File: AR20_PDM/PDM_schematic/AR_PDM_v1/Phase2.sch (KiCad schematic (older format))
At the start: 10 parts, among them Q6 BTS50025-1TAD, U6 INA233

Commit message: Working on pcb layout
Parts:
- removed D?: D_Schottky_x2, symbol AR20_PDM_v1-rescue:D_Schottky_x2
- added D51, D52: D_Schottky_BAT60A, AR_PDM_v1:D_Shotky_BAT60_HandSoldering, symbol AR20_PDM_v1-rescue:D_Schottky_BAT60A
- gave numbers to parts that had none: 4
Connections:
- net GND: now also D51.2 (A), D52.2 (A)
- net at R113.1, U6.10 (IN+): now also D52.1 (K)
- net at R111.1, U6.9 (In-): now also D51.1 (K)
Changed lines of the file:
@@
 AR Path="/5E0E594B/5EE88A56" Ref="R?"  Part="1"
 AR Path="/5E0E607C/5EE88A56" Ref="R?"  Part="1"
-AR Path="/5E0FB5C8/5EE88A56" Ref="R?"  Part="1"
+AR Path="/5E0FB5C8/5EE88A56" Ref="R112"  Part="1"
 AR Path="/5E0FBBBD/5EE88A56" Ref="R?"  Part="1"
 AR Path="/5E0FC3A2/5EE88A56" Ref="R?"  Part="1"
@@
 AR Path="/5E0FDCCC/5EE88A56" Ref="R?"  Part="1"
 AR Path="/5E10174B/5EE88A56" Ref="R?"  Part="1"
-F 0 "R?" V 6643 1600 50  0000 C CNN
+F 0 "R112" V 6643 1600 50  0000 C CNN
 F 1 "2m_1%_4W" V 6734 1600 50  0000 C CNN
 F 2 "Resistor_SMD:R_2512_6332Metric" V 6780 1600 50  0001 C CNN
@@
 Text HLabel 7300 1600 2    50   Input ~ 10
 V+12V
-$Comp
-L AR20_PDM_v1-rescue:D_Schottky_x2 D?
-U 1 1 5EE88A5D
-P 6950 4825
-AR Path="/5DA89415/5EE88A5D" Ref="D?"  Part="1"
-AR Path="/5E0FB5C8/5EE88A5D" Ref="D?"  Part="1"
-F 0 "D?" H 6950 5041 50  0000 C CNN
-F 1 "D_Schottky_x2" H 6950 4950 50  0000 C CNN
-F 2 "" H 6950 4825 50  0001 C CNN
-F 3 "~" H 6950 4825 50  0001 C CNN
-	1    6950 4825
-	1    0    0    -1
-$EndComp
 $Comp
 L AR20_PDM_v1-rescue:R-Device R?
@@
 AR Path="/5E0E594B/5EE88A63" Ref="R?"  Part="1"
 AR Path="/5E0E607C/5EE88A63" Ref="R?"  Part="1"
-AR Path="/5E0FB5C8/5EE88A63" Ref="R?"  Part="1"
+AR Path="/5E0FB5C8/5EE88A63" Ref="R111"  Part="1"
 AR Path="/5E0FBBBD/5EE88A63" Ref="R?"  Part="1"
 AR Path="/5E0FC3A2/5EE88A63" Ref="R?"  Part="1"
@@
 AR Path="/5E0FDCCC/5EE88A63" Ref="R?"  Part="1"
 AR Path="/5E10174B/5EE88A63" Ref="R?"  Part="1"
-F 0 "R?" V 6443 3850 50  0000 C CNN
+F 0 "R111" V 6443 3850 50  0000 C CNN
 F 1 "1K_1%" V 6534 3850 50  0000 C CNN
 F 2 "Resistor_SMD:R_0603_1608Metric" V 6580 3850 50  0001 C CNN
@@
 AR Path="/5E0E594B/5EE88A69" Ref="R?"  Part="1"
 AR Path="/5E0E607C/5EE88A69" Ref="R?"  Part="1"
-AR Path="/5E0FB5C8/5EE88A69" Ref="R?"  Part="1"
+AR Path="/5E0FB5C8/5EE88A69" Ref="R113"  Part="1"
 AR Path="/5E0FBBBD/5EE88A69" Ref="R?"  Part="1"
 AR Path="/5E0FC3A2/5EE88A69" Ref="R?"  Part="1"
@@
 AR Path="/5E0FDCCC/5EE88A69" Ref="R?"  Part="1"
 AR Path="/5E10174B/5EE88A69" Ref="R?"  Part="1"
-F 0 "R?" V 6843 3850 50  0000 C CNN
+F 0 "R113" V 6843 3850 50  0000 C CNN
 F 1 "1K_1%" V 6934 3850 50  0000 C CNN
 F 2 "Resistor_SMD:R_0603_1608Metric" V 6980 3850 50  0001 C CNN
@@
 Text Notes 7075 2000 0    50   ~ 10
 Place shunt and INA233 close, \nroute togethere, differentialy pair. \nKeep short, and away from Noise.
-$Comp
-L AR20_PDM_v1-rescue:GND-power #PWR?
-U 1 1 5EE88A77
-P 6950 5025
-AR Path="/5DA89415/5EE88A77" Ref="#PWR?"  Part="1"
-AR Path="/5DEB10A1/5EE88A77" Ref="#PWR?"  Part="1"
-AR Path="/5DEB20EA/5EE88A77" Ref="#PWR?"  Part="1"
-AR Path="/5E0E4725/5EE88A77" Ref="#PWR?"  Part="1"
-AR Path="/5E0E4A93/5EE88A77" Ref="#PWR?"  Part="1"
-AR Path="/5E0E4EB5/5EE88A77" Ref="#PWR?"  Part="1"
-AR Path="/5E0E5304/5EE88A77" Ref="#PWR?"  Part="1"
-AR Path="/5E0E594B/5EE88A77" Ref="#PWR?"  Part="1"
-AR Path="/5E0E607C/5EE88A77" Ref="#PWR?"  Part="1"
-AR Path="/5E0FB5C8/5EE88A77" Ref="#PWR?"  Part="1"
-AR Path="/5E0FBBBD/5EE88A77" Ref="#PWR?"  Part="1"
-AR Path="/5E0FC3A2/5EE88A77" Ref="#PWR?"  Part="1"
-AR Path="/5E0FCFDC/5EE88A77" Ref="#PWR?"  Part="1"
-AR Path="/5E0FDCCC/5EE88A77" Ref="#PWR?"  Part="1"
-AR Path="/5E10174B/5EE88A77" Ref="#PWR?"  Part="1"
-F 0 "#PWR?" H 6950 4775 50  0001 C CNN
-F 1 "GND" H 6955 4852 50  0000 C CNN
-F 2 "" H 6950 5025 50  0001 C CNN
-F 3 "" H 6950 5025 50  0001 C CNN
-	1    6950 5025
-	1    0    0    -1
-$EndComp
 Wire Wire Line
 	4775 1600 6650 1600
@@
 Wire Wire Line
 	6650 4400 8750 4400
-Connection ~ 6650 4400
-Wire Wire Line
-	6650 4400 6650 4825
-Wire Wire Line
-	8750 4300 7250 4300
-Wire Wire Line
-	7250 4825 7250 4300
-Connection ~ 7250 4300
-Wire Wire Line
-	7250 4300 7050 4300
 $Comp
 L AR20_PDM_v1-rescue:R-Device R?
@@
 AR Path="/5E0E594B/5EEC0C80" Ref="R?"  Part="1"
 AR Path="/5E0E607C/5EEC0C80" Ref="R?"  Part="1"
-AR Path="/5E0FB5C8/5EEC0C80" Ref="R?"  Part="1"
+AR Path="/5E0FB5C8/5EEC0C80" Ref="R114"  Part="1"
 AR Path="/5E0FBBBD/5EEC0C80" Ref="R?"  Part="1"
 AR Path="/5E0FC3A2/5EEC0C80" Ref="R?"  Part="1"
@@
 AR Path="/5E0FDCCC/5EEC0C80" Ref="R?"  Part="1"
 AR Path="/5E10174B/5EEC0C80" Ref="R?"  Part="1"
-F 0 "R?" V 8093 4100 50  0000 C CNN
+F 0 "R114" V 8093 4100 50  0000 C CNN
 F 1 "10K" V 8184 4100 50  0000 C CNN
 F 2 "Resistor_SMD:R_0603_1608Metric" V 8230 4100 50  0001 C CNN
@@
 Text HLabel 8150 4100 0    50   Output ~ 10
 P2_OUT
+Wire Wire Line
+	7050 4300 7100 4300
+$Comp
+L AR20_PDM_v1-rescue:D_Schottky_BAT60A D?
+U 1 1 5EFA1E07
+P 6700 4775
+AR Path="/5DA89415/5EFA1E07" Ref="D?"  Part="1"
+AR Path="/5E0FB5C8/5EFA1E07" Ref="D51"  Part="1"
+F 0 "D51" V 6530 4885 50  0000 L CNN
+F 1 "D_Schottky_BAT60A" V 6621 4885 50  0000 L CNN
+F 2 "AR_PDM_v1:D_Shotky_BAT60_HandSoldering" H 6800 4725 50  0001 C CNN
+F 3 "~" H 6800 4725 50  0001 C CNN
+	1    6700 4775
+	0    1    1    0
+$EndComp
+$Comp
+L AR20_PDM_v1-rescue:GND-power #PWR?
+U 1 1 5EFA1E0D
+P 6875 4950
+AR Path="/5DA89415/5EFA1E0D" Ref="#PWR?"  Part="1"
+AR Path="/5DEB10A1/5EFA1E0D" Ref="#PWR?"  Part="1"
+AR Path="/5DEB20EA/5EFA1E0D" Ref="#PWR?"  Part="1"
+AR Path="/5E0E4725/5EFA1E0D" Ref="#PWR?"  Part="1"
+AR Path="/5E0E4A93/5EFA1E0D" Ref="#PWR?"  Part="1"
+AR Path="/5E0E4EB5/5EFA1E0D" Ref="#PWR?"  Part="1"
+AR Path="/5E0E5304/5EFA1E0D" Ref="#PWR?"  Part="1"
+AR Path="/5E0E594B/5EFA1E0D" Ref="#PWR?"  Part="1"
+AR Path="/5E0E607C/5EFA1E0D" Ref="#PWR?"  Part="1"
+AR Path="/5E0FB5C8/5EFA1E0D" Ref="#PWR013"  Part="1"
+AR Path="/5E0FBBBD/5EFA1E0D" Ref="#PWR?"  Part="1"
+AR Path="/5E0FC3A2/5EFA1E0D" Ref="#PWR?"  Part="1"
+AR Path="/5E0FCFDC/5EFA1E0D" Ref="#PWR?"  Part="1"
+AR Path="/5E0FDCCC/5EFA1E0D" Ref="#PWR?"  Part="1"
+AR Path="/5E10174B/5EFA1E0D" Ref="#PWR?"  Part="1"
+F 0 "#PWR013" H 6875 4700 50  0001 C CNN
+F 1 "GND" H 6880 4777 50  0000 C CNN
+F 2 "" H 6875 4950 50  0001 C CNN
+F 3 "" H 6875 4950 50  0001 C CNN
+	1    6875 4950
+	1    0    0    -1
+$EndComp
+$Comp
+L AR20_PDM_v1-rescue:D_Schottky_BAT60A D?
+U 1 1 5EFA1E13
+P 7150 4775
+AR Path="/5DA89415/5EFA1E13" Ref="D?"  Part="1"
+AR Path="/5E0FB5C8/5EFA1E13" Ref="D52"  Part="1"
+F 0 "D52" V 6980 4885 50  0000 L CNN
+F 1 "D_Schottky_BAT60A" V 7071 4885 50  0000 L CNN
+F 2 "AR_PDM_v1:D_Shotky_BAT60_HandSoldering" H 7250 4725 50  0001 C CNN
+F 3 "~" H 7250 4725 50  0001 C CNN
+	1    7150 4775
+	0    1    1    0
+$EndComp
+Wire Wire Line
+	6650 4475 6650 4400
+Wire Wire Line
+	7100 4475 7100 4300
+Wire Wire Line
+	6650 4825 6875 4825
+Wire Wire Line
+	6875 4950 6875 4825
+Connection ~ 6875 4825
+Wire Wire Line
+	6875 4825 7100 4825
+Connection ~ 7100 4300
+Wire Wire Line
+	7100 4300 8750 4300
+Connection ~ 6650 4400
 $EndSCHEMATC

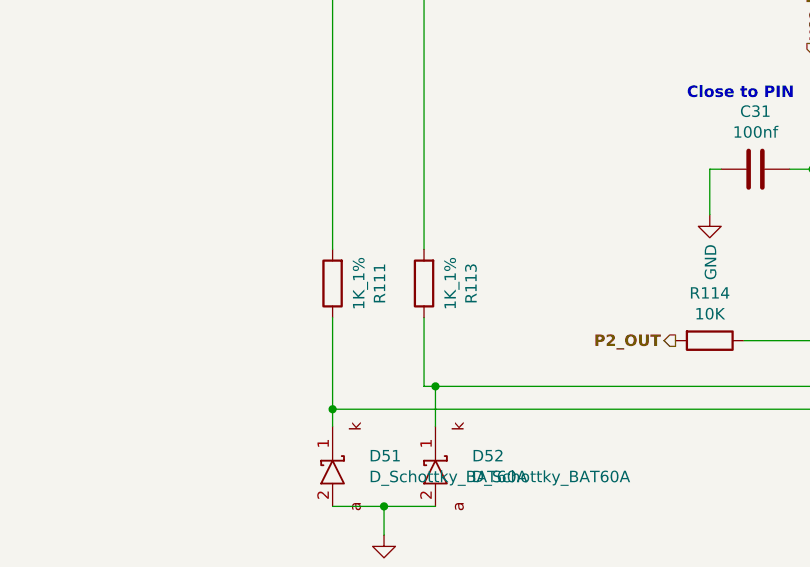
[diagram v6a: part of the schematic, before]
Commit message: shematics adjustments, and fixing values and names
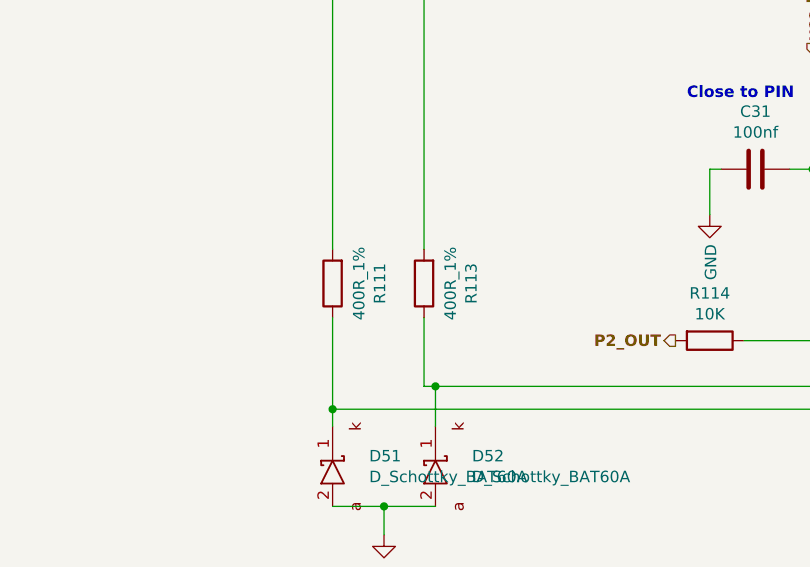
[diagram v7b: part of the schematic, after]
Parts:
- R111, R113: value 1K_1% -> 400R_1%
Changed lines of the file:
@@
 AR Path="/5E10174B/5EE88A63" Ref="R?"  Part="1"
 F 0 "R111" V 6443 3850 50  0000 C CNN
-F 1 "1K_1%" V 6534 3850 50  0000 C CNN
+F 1 "400R_1%" V 6534 3850 50  0000 C CNN
 F 2 "Resistor_SMD:R_0603_1608Metric" V 6580 3850 50  0001 C CNN
 F 3 "~" H 6650 3850 50  0001 C CNN
@@
 AR Path="/5E10174B/5EE88A69" Ref="R?"  Part="1"
 F 0 "R113" V 6843 3850 50  0000 C CNN
-F 1 "1K_1%" V 6934 3850 50  0000 C CNN
+F 1 "400R_1%" V 6934 3850 50  0000 C CNN
 F 2 "Resistor_SMD:R_0603_1608Metric" V 6980 3850 50  0001 C CNN
 F 3 "~" H 7050 3850 50  0001 C CNN
